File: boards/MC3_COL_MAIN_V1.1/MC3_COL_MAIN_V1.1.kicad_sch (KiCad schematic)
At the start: 9 parts

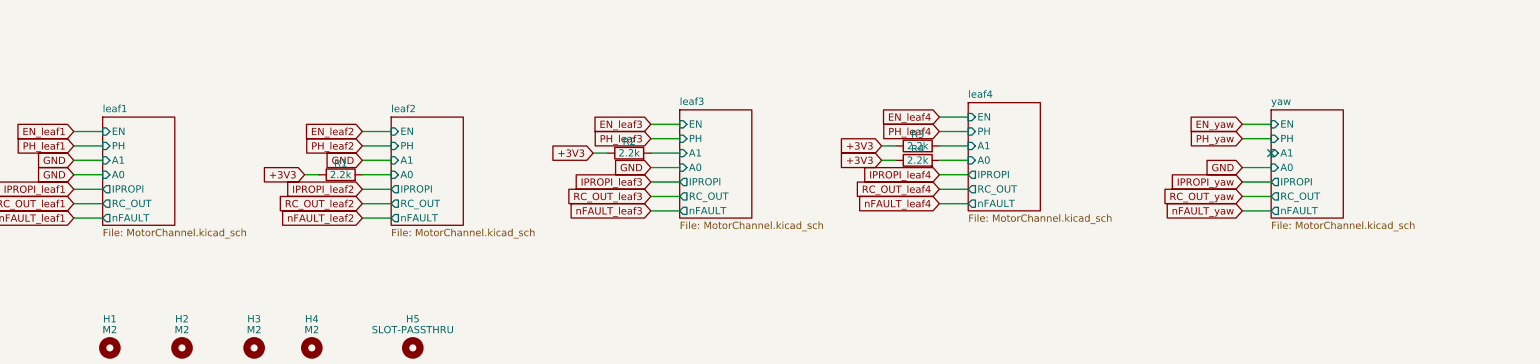
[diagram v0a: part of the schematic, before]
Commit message: V1.1: J13 machine-harness FFC (TE 84952-6, 1.0 mm 6-way) - YAW_OUT1/2 via new OUT1/OUT2 sheet pins, VIN_PAD/GND/CANH/CANL; ERC 0 errors
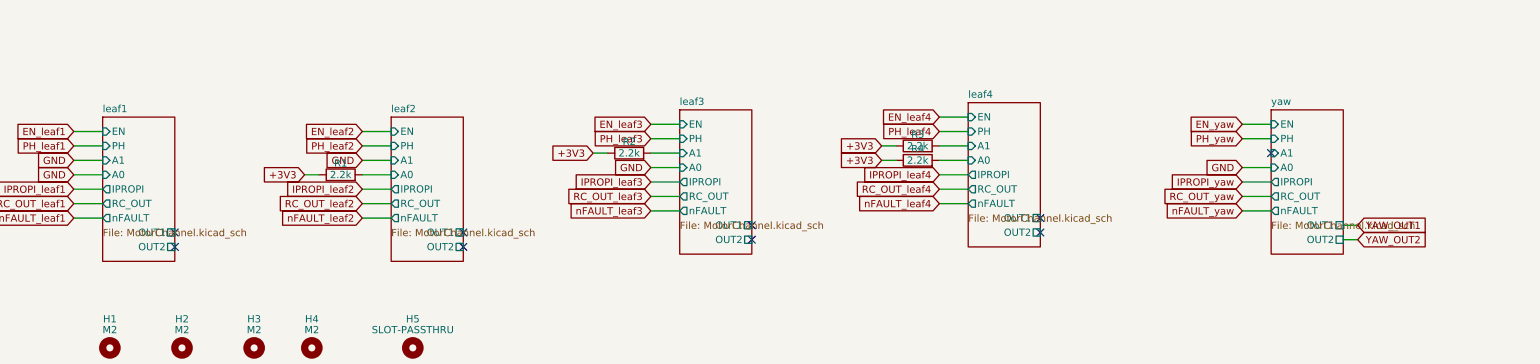
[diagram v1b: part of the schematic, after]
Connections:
- no-connect marks 1 -> 9
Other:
- sheet leaf1 ports: added OUT1, OUT2; removed none
- sheet leaf2 ports: added OUT1, OUT2; removed none
- sheet leaf3 ports: added OUT1, OUT2; removed none
- sheet leaf4 ports: added OUT1, OUT2; removed none
- sheet yaw ports: added OUT1, OUT2; removed none

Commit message: V1.1: encoder connector nets swapped to match placement (J3=leaf2, J4=leaf1, J5=leaf4, J6=leaf3)
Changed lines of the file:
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@@
 		(on_board yes)
 		(dnp no)
-		(fields_autoplaced yes)
 		(stroke
 			(width 0.1524)
@@
 		)
 		(property "Sheetfile" "MotorChannel.kicad_sch"
-			(at 90.17 89.4846 0)
+			(at 84.328 97.79 0)
 			(show_name no)
 			(do_not_autoplace no)
@@
 		(on_board yes)
 		(dnp no)
-		(fields_autoplaced yes)
 		(stroke
 			(width 0.1524)
@@
 		)
 		(property "Sheetfile" "MotorChannel.kicad_sch"
-			(at 245.11 88.2146 0)
+			(at 239.014 96.012 0)
 			(show_name no)
 			(do_not_autoplace no)
@@
 		(on_board yes)
 		(dnp no)
-		(fields_autoplaced yes)
 		(stroke
 			(width 0.1524)
@@
 		)
 		(property "Sheetfile" "MotorChannel.kicad_sch"
-			(at 191.77 86.9446 0)
+			(at 184.404 95.504 0)
 			(show_name no)
 			(do_not_autoplace no)
@@
 		(on_board yes)
 		(dnp no)
-		(fields_autoplaced yes)
 		(stroke
 			(width 0.1524)
@@
 		)
 		(property "Sheetfile" "MotorChannel.kicad_sch"
-			(at 39.37 89.4846 0)
+			(at 34.798 97.536 0)
 			(show_name no)
 			(do_not_autoplace no)
@@
 		(on_board yes)
 		(dnp no)
-		(fields_autoplaced yes)
 		(stroke
 			(width 0.1524)
@@
 		)
 		(property "Sheetfile" "MotorChannel.kicad_sch"
-			(at 140.97 88.2146 0)
-			(show_name no)
-			(do_not_autoplace no)
+			(at 135.382 95.504 0)
+			(show_name no)
+			(do_not_autoplace no)
